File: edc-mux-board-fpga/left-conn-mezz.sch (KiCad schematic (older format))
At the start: 80 parts, among them J13 Device 0, J14 Device 1, J15 Device 2, J16 Device 3, J17 Device 4, J18 Device 5, J19 Left Mezzanine Board Connecto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, J20 Left Mezzanine Board Connecto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

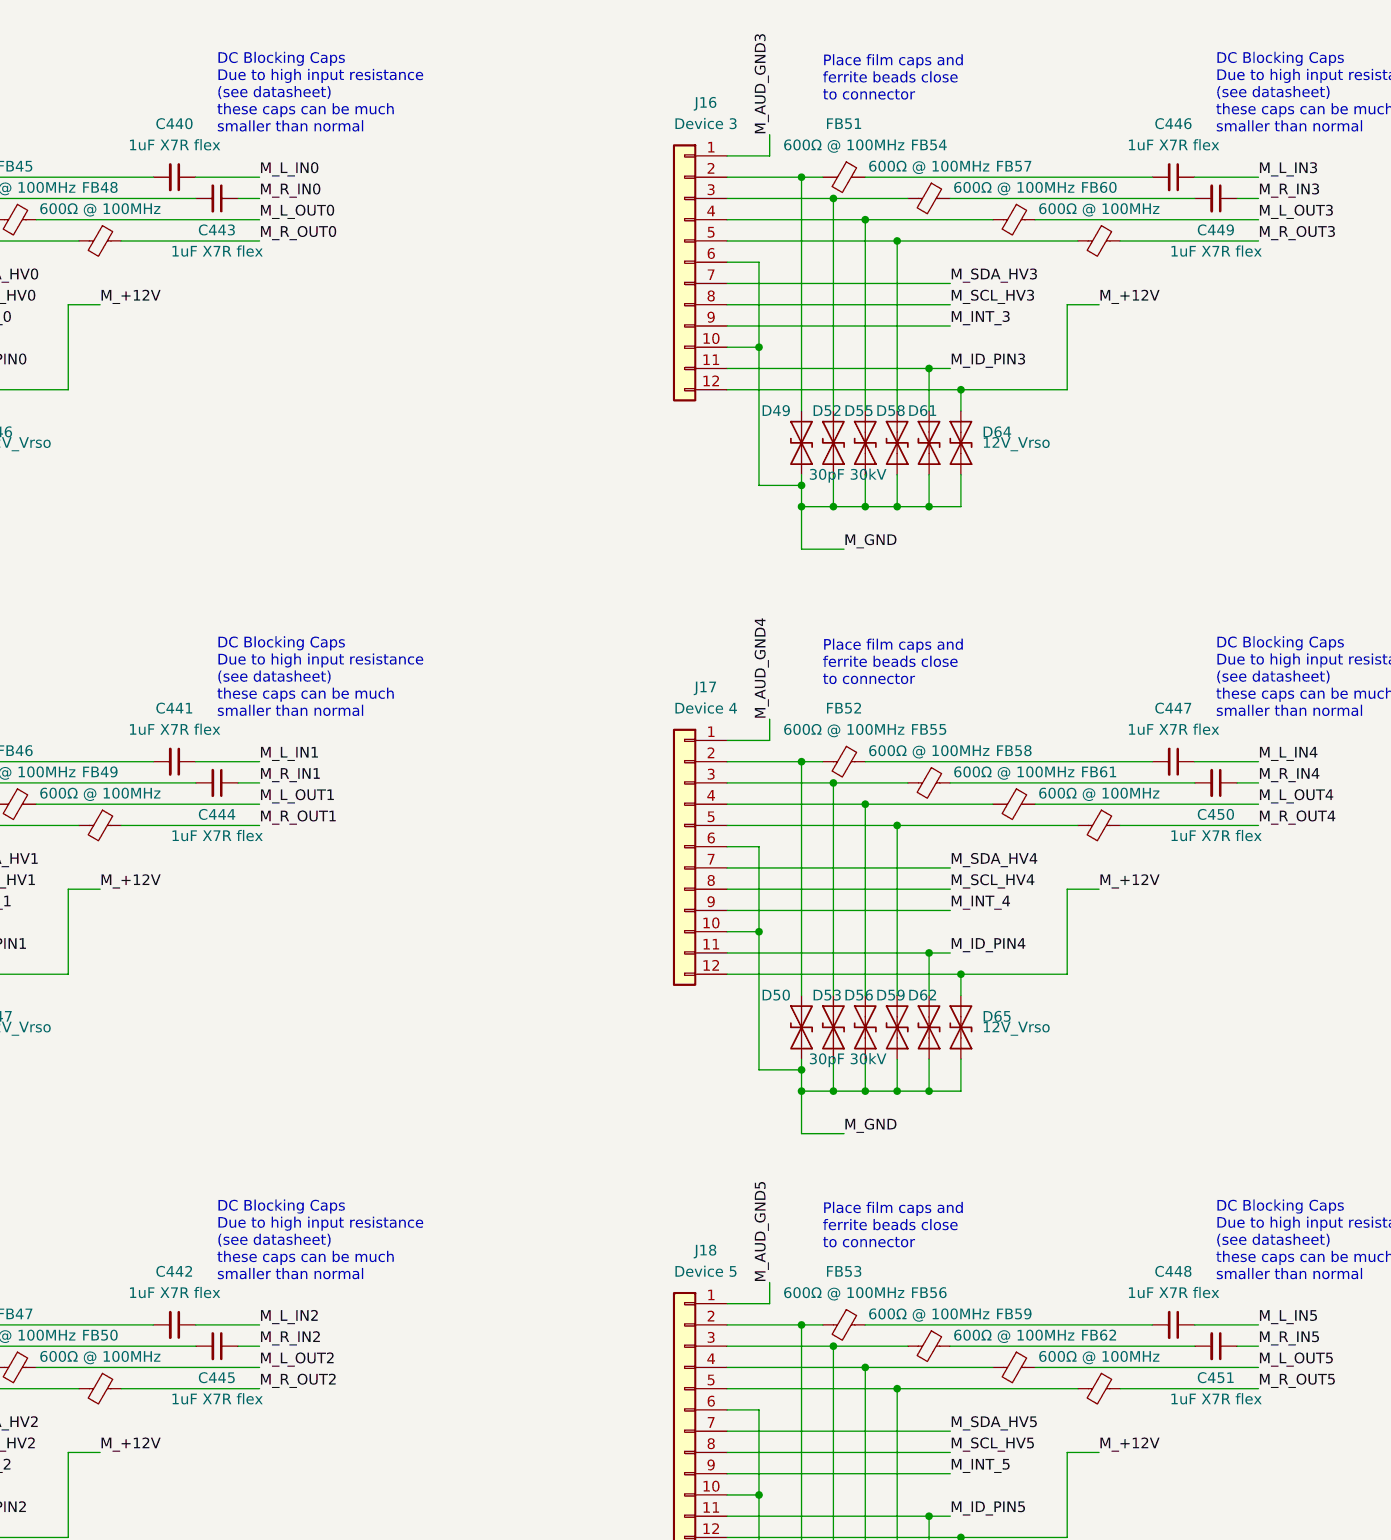
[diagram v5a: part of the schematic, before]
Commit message: Reannotating and adding more fields to components
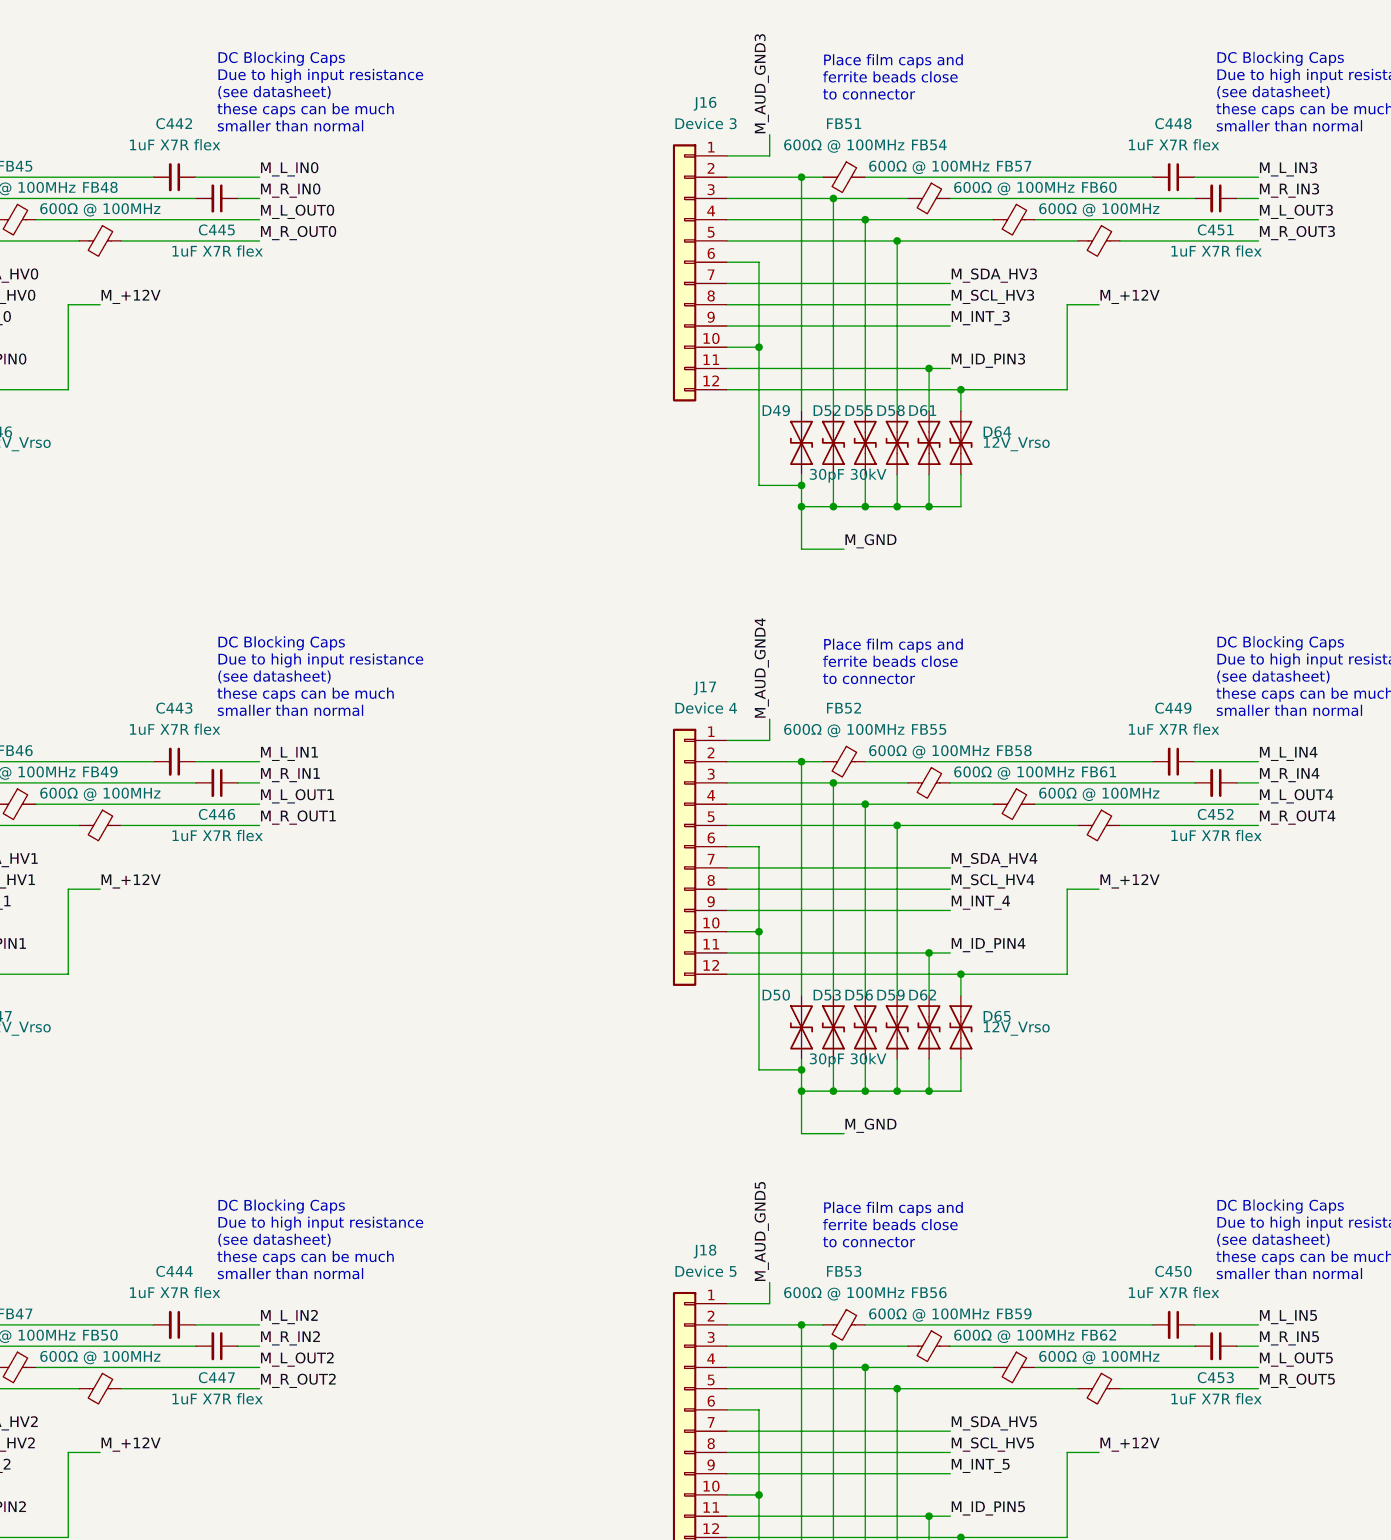
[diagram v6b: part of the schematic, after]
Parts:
- C442: renamed from C440; Characteristics (none) -> CAP CER 0805 1UF 25V X7R 5%; Description (none) -> MLCC Capacitor; Manufacturers Part Number C0805X105J3RACAUTO -> C0805X105J3RECAUTO
- C443: renamed from C441; Characteristics (none) -> CAP CER 0805 1UF 25V X7R 5%; Description (none) -> MLCC Capacitor; Manufacturers Part Number C0805X105J3RACAUTO -> C0805X105J3RECAUTO
- C444: renamed from C442; Characteristics (none) -> CAP CER 0805 1UF 25V X7R 5%; Description (none) -> MLCC Capacitor; Manufacturers Part Number C0805X105J3RACAUTO -> C0805X105J3RECAUTO
- C445: renamed from C443; Characteristics (none) -> CAP CER 0805 1UF 25V X7R 5%; Description (none) -> MLCC Capacitor; Manufacturers Part Number C0805X105J3RACAUTO -> C0805X105J3RECAUTO
- C446: renamed from C444; Characteristics (none) -> CAP CER 0805 1UF 25V X7R 5%; Description (none) -> MLCC Capacitor; Manufacturers Part Number C0805X105J3RACAUTO -> C0805X105J3RECAUTO
- C447: renamed from C445; Characteristics (none) -> CAP CER 0805 1UF 25V X7R 5%; Description (none) -> MLCC Capacitor; Manufacturers Part Number C0805X105J3RACAUTO -> C0805X105J3RECAUTO
- C448: renamed from C446; Characteristics (none) -> CAP CER 0805 1UF 25V X7R 5%; Description (none) -> MLCC Capacitor; Manufacturers Part Number C0805X105J3RACAUTO -> C0805X105J3RECAUTO
- C449: renamed from C447; Characteristics (none) -> CAP CER 0805 1UF 25V X7R 5%; Description (none) -> MLCC Capacitor; Manufacturers Part Number C0805X105J3RACAUTO -> C0805X105J3RECAUTO
- C450: renamed from C448; Characteristics (none) -> CAP CER 0805 1UF 25V X7R 5%; Description (none) -> MLCC Capacitor; Manufacturers Part Number C0805X105J3RACAUTO -> C0805X105J3RECAUTO
- C451: renamed from C449; Characteristics (none) -> CAP CER 0805 1UF 25V X7R 5%; Description (none) -> MLCC Capacitor; Manufacturers Part Number C0805X105J3RACAUTO -> C0805X105J3RECAUTO
- C452: renamed from C450; Characteristics (none) -> CAP CER 0805 1UF 25V X7R 5%; Description (none) -> MLCC Capacitor; Manufacturers Part Number C0805X105J3RACAUTO -> C0805X105J3RECAUTO
- C453: renamed from C451; Characteristics (none) -> CAP CER 0805 1UF 25V X7R 5%; Description (none) -> MLCC Capacitor; Manufacturers Part Number C0805X105J3RACAUTO -> C0805X105J3RECAUTO
- FB39, FB40, FB41, FB42, FB43, FB44, FB45, FB46, FB47, FB48, FB49, FB50, FB51, FB52, FB53, FB54, FB55, FB56, FB57, FB58, FB59, FB60, FB61, FB62: footprint Capacitor_SMD:C_0805_2012Metric -> Inductor_SMD:L_0805_2012Metric; Characteristics (none) -> 600 Ohms @ 100MHz 1 Signal Line Ferrite Bead 0805 (2012 Met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; Description (none) -> Ferrite Bead; Manufacturers Part Number BLM21AG601BH1 -> BLM21AG601SZ1D
- J13, J14, J15, J16, J17, J18: Description (none) -> M12 A Coded 12 Pin Connector; Package ID (none) -> Through Hole
- J19, J20: Package ID (none) -> Through Hole

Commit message: Fixed pin header footprint issues
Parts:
- J19: footprint Connector_PinSocket_2.54mm:PinSocket_2x10_P2.54mm_Horizontal -> Connector_PinSocket_2.54mm:PinSocket_2x40_P2.54mm_Horizontal
- J20: footprint Connector_PinHeader_2.54mm:PinHeader_2x10_P2.54mm_Vertical -> Connector_PinHeader_2.54mm:PinHeader_2x40_P2.54mm_Vertical
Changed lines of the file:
@@
 F 0 "J19" H 10400 6950 50  0000 C CNN
 F 1 "Left Mezzanine Board Connector (Daughterboard)" H 10400 2850 50  0000 C CNN
-F 2 "Connector_PinSocket_2.54mm:PinSocket_2x10_P2.54mm_Horizontal" H 10350 4950 50  0001 C CNN
+F 2 "Connector_PinSocket_2.54mm:PinSocket_2x40_P2.54mm_Horizontal" H 10350 4950 50  0001 C CNN
 F 3 "~" H 10350 4950 50  0001 C CNN
 F 4 "Through Hole" H 0   0   50  0001 C CNN "Package ID"
@@
 F 0 "J20" H 13950 6950 50  0000 C CNN
 F 1 "Left Mezzanine Board Connector (Motherboard)" H 13950 2850 50  0000 C CNN
-F 2 "Connector_PinHeader_2.54mm:PinHeader_2x10_P2.54mm_Vertical" H 13900 4950 50  0001 C CNN
+F 2 "Connector_PinHeader_2.54mm:PinHeader_2x40_P2.54mm_Vertical" H 13900 4950 50  0001 C CNN
 F 3 "~" H 13900 4950 50  0001 C CNN
 F 4 "Through Hole" H 0   0   50  0001 C CNN "Package ID"

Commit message: Reannotating board
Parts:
- renumbered C442 to C441, C443 to C442, C444 to C443, C445 to C444, C446 to C445, C447 to C446, C448 to C447, C449 to C448, C450 to C449, C451 to C450, C452 to C451, C453 to C452, D31 to D28, D32 to D29, D33 to D30, D34 to D31, D35 to D32, D36 to D33, D37 to D34, D38 to D35, D39 to D36, D40 to D37, D41 to D38, D42 to D39, D43 to D40, D44 to D41, D45 to D42, D46 to D43, D47 to D44, D48 to D45, D49 to D46, D50 to D47, D51 to D48, D52 to D49, D53 to D50, D54 to D51, D55 to D52, D56 to D53, D57 to D54, D58 to D55, D59 to D56, D60 to D57, D61 to D58, D62 to D59, D63 to D60, D64 to D61, D65 to D62, D66 to D63, FB39 to FB38, FB40 to FB39, FB41 to FB40, FB42 to FB41, FB43 to FB42, FB44 to FB43, FB45 to FB44, FB46 to FB45, FB47 to FB46, FB48 to FB47, FB49 to FB48, FB50 to FB49, FB51 to FB50, FB52 to FB51, FB53 to FB52, FB54 to FB53, FB55 to FB54, FB56 to FB55, FB57 to FB56, FB58 to FB57, FB59 to FB58, FB60 to FB59, FB61 to FB60, FB62 to FB61, J13 to J12, J14 to J13, J15 to J14, J16 to J15, J17 to J16, J18 to J17, J19 to J18, J20 to J19
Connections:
- net M_+12V: now also J18.35 (Pin_35), J18.36 (Pin_36); no longer J18.43 (Pin_43), J18.44 (Pin_44)
- net M_AUD_GND0: now also J18.3 (Pin_3); no longer J18.5 (Pin_5)
- net M_AUD_GND1: now also J18.15 (Pin_15); no longer J18.17 (Pin_17)
- net M_AUD_GND2: now also J18.27 (Pin_27); no longer J18.29 (Pin_29)
- net M_AUD_GND3: now also J18.49 (Pin_49); no longer J18.51 (Pin_51)
- net M_AUD_GND4: now also J18.61 (Pin_61); no longer J18.63 (Pin_63)
- net M_AUD_GND5: now also J18.73 (Pin_73); no longer J18.75 (Pin_75)
- net M_GND: now also J18.10 (Pin_10), J18.16 (Pin_16), J18.21 (Pin_21), J18.22 (Pin_22), J18.28 (Pin_28), J18.33 (Pin_33), J18.34 (Pin_34), J18.4 (Pin_4), J18.43 (Pin_43), J18.44 (Pin_44), J18.50 (Pin_50), J18.55 (Pin_55), J18.56 (Pin_56), J18.62 (Pin_62), J18.67 (Pin_67), J18.68 (Pin_68), J18.74 (Pin_74), J18.9 (Pin_9); no longer J18.11 (Pin_11), J18.12 (Pin_12), J18.18 (Pin_18), J18.23 (Pin_23), J18.24 (Pin_24), J18.30 (Pin_30), J18.35 (Pin_35), J18.36 (Pin_36), J18.45 (Pin_45), J18.46 (Pin_46), J18.52 (Pin_52), J18.57 (Pin_57), J18.58 (Pin_58), J18.6 (Pin_6), J18.64 (Pin_64), J18.69 (Pin_69), J18.70 (Pin_70), J18.76 (Pin_76)
- net M_ID_PIN0: now also J18.7 (Pin_7); no longer J18.9 (Pin_9)
- net M_ID_PIN1: now also J18.19 (Pin_19); no longer J18.21 (Pin_21)
- net M_ID_PIN2: now also J18.31 (Pin_31); no longer J18.33 (Pin_33)
- net M_ID_PIN3: now also J18.53 (Pin_53); no longer J18.55 (Pin_55)
- net M_ID_PIN4: now also J18.65 (Pin_65); no longer J18.67 (Pin_67)
- net M_ID_PIN5: now also J18.77 (Pin_77); no longer J18.79 (Pin_79)
- net M_INT_0: now also J18.5 (Pin_5); no longer J18.7 (Pin_7)
- net M_INT_1: now also J18.17 (Pin_17); no longer J18.19 (Pin_19)
- net M_INT_2: now also J18.29 (Pin_29); no longer J18.31 (Pin_31)
- net M_INT_3: now also J18.51 (Pin_51); no longer J18.53 (Pin_53)
- net M_INT_4: now also J18.63 (Pin_63); no longer J18.65 (Pin_65)
- net M_INT_5: now also J18.75 (Pin_75); no longer J18.77 (Pin_77)
- net M_L_IN0: now also J18.1 (Pin_1); no longer J18.3 (Pin_3)
- net M_L_IN1: now also J18.13 (Pin_13); no longer J18.15 (Pin_15)
- net M_L_IN2: now also J18.25 (Pin_25); no longer J18.27 (Pin_27)
- net M_L_IN3: now also J18.47 (Pin_47); no longer J18.49 (Pin_49)
- net M_L_IN4: now also J18.59 (Pin_59); no longer J18.61 (Pin_61)
- net M_L_IN5: now also J18.71 (Pin_71); no longer J18.73 (Pin_73)
- net M_L_OUT0: no longer J18.2 (Pin_2)
- net M_L_OUT1: now also J18.14 (Pin_14); no longer J18.16 (Pin_16)
- net M_L_OUT2: now also J18.26 (Pin_26); no longer J18.28 (Pin_28)
- net M_L_OUT3: now also J18.48 (Pin_48); no longer J18.50 (Pin_50)
- net M_L_OUT4: now also J18.60 (Pin_60); no longer J18.62 (Pin_62)
- net M_L_OUT5: now also J18.72 (Pin_72); no longer J18.74 (Pin_74)
- net M_R_IN0: no longer J18.1 (Pin_1)
- net M_R_IN1: now also J18.11 (Pin_11); no longer J18.13 (Pin_13)
- net M_R_IN2: now also J18.23 (Pin_23); no longer J18.25 (Pin_25)
- net M_R_IN3: now also J18.45 (Pin_45); no longer J18.47 (Pin_47)
- net M_R_IN4: now also J18.57 (Pin_57); no longer J18.59 (Pin_59)
- net M_R_IN5: now also J18.69 (Pin_69); no longer J18.71 (Pin_71)
- net M_R_OUT0: now also J18.2 (Pin_2); no longer J18.4 (Pin_4)
- net M_R_OUT1: now also J18.12 (Pin_12); no longer J18.14 (Pin_14)
- net M_R_OUT2: now also J18.24 (Pin_24); no longer J18.26 (Pin_26)
- net M_R_OUT3: now also J18.46 (Pin_46); no longer J18.48 (Pin_48)
- net M_R_OUT4: now also J18.58 (Pin_58); no longer J18.60 (Pin_60)
- net M_R_OUT5: now also J18.70 (Pin_70); no longer J18.72 (Pin_72)
- net M_SCL_HV0: now also J18.6 (Pin_6); no longer J18.8 (Pin_8)
- net M_SCL_HV1: now also J18.18 (Pin_18); no longer J18.20 (Pin_20)
- net M_SCL_HV2: now also J18.30 (Pin_30); no longer J18.32 (Pin_32)
- net M_SCL_HV3: now also J18.52 (Pin_52); no longer J18.54 (Pin_54)
- net M_SCL_HV4: now also J18.64 (Pin_64); no longer J18.66 (Pin_66)
- net M_SCL_HV5: now also J18.76 (Pin_76); no longer J18.78 (Pin_78)
- net M_SDA_HV0: now also J18.8 (Pin_8); no longer J18.10 (Pin_10)
- net M_SDA_HV1: now also J18.20 (Pin_20); no longer J18.22 (Pin_22)
- net M_SDA_HV2: now also J18.32 (Pin_32); no longer J18.34 (Pin_34)
- net M_SDA_HV3: now also J18.54 (Pin_54); no longer J18.56 (Pin_56)
- net M_SDA_HV4: now also J18.66 (Pin_66); no longer J18.68 (Pin_68)
- net M_SDA_HV5: now also J18.78 (Pin_78); no longer J18.80 (Pin_80)
